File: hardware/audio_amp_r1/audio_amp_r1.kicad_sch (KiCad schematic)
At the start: 24 parts, among them J1 PJ-320D, J2 PJ-320D, J3 JST_PH_1x02, J4 Conn_01x04_Pin, J5 Conn_01x04_Pin, J6 KH-BNC50-3511, J7 KH-BNC50-3511, U1 AD8397

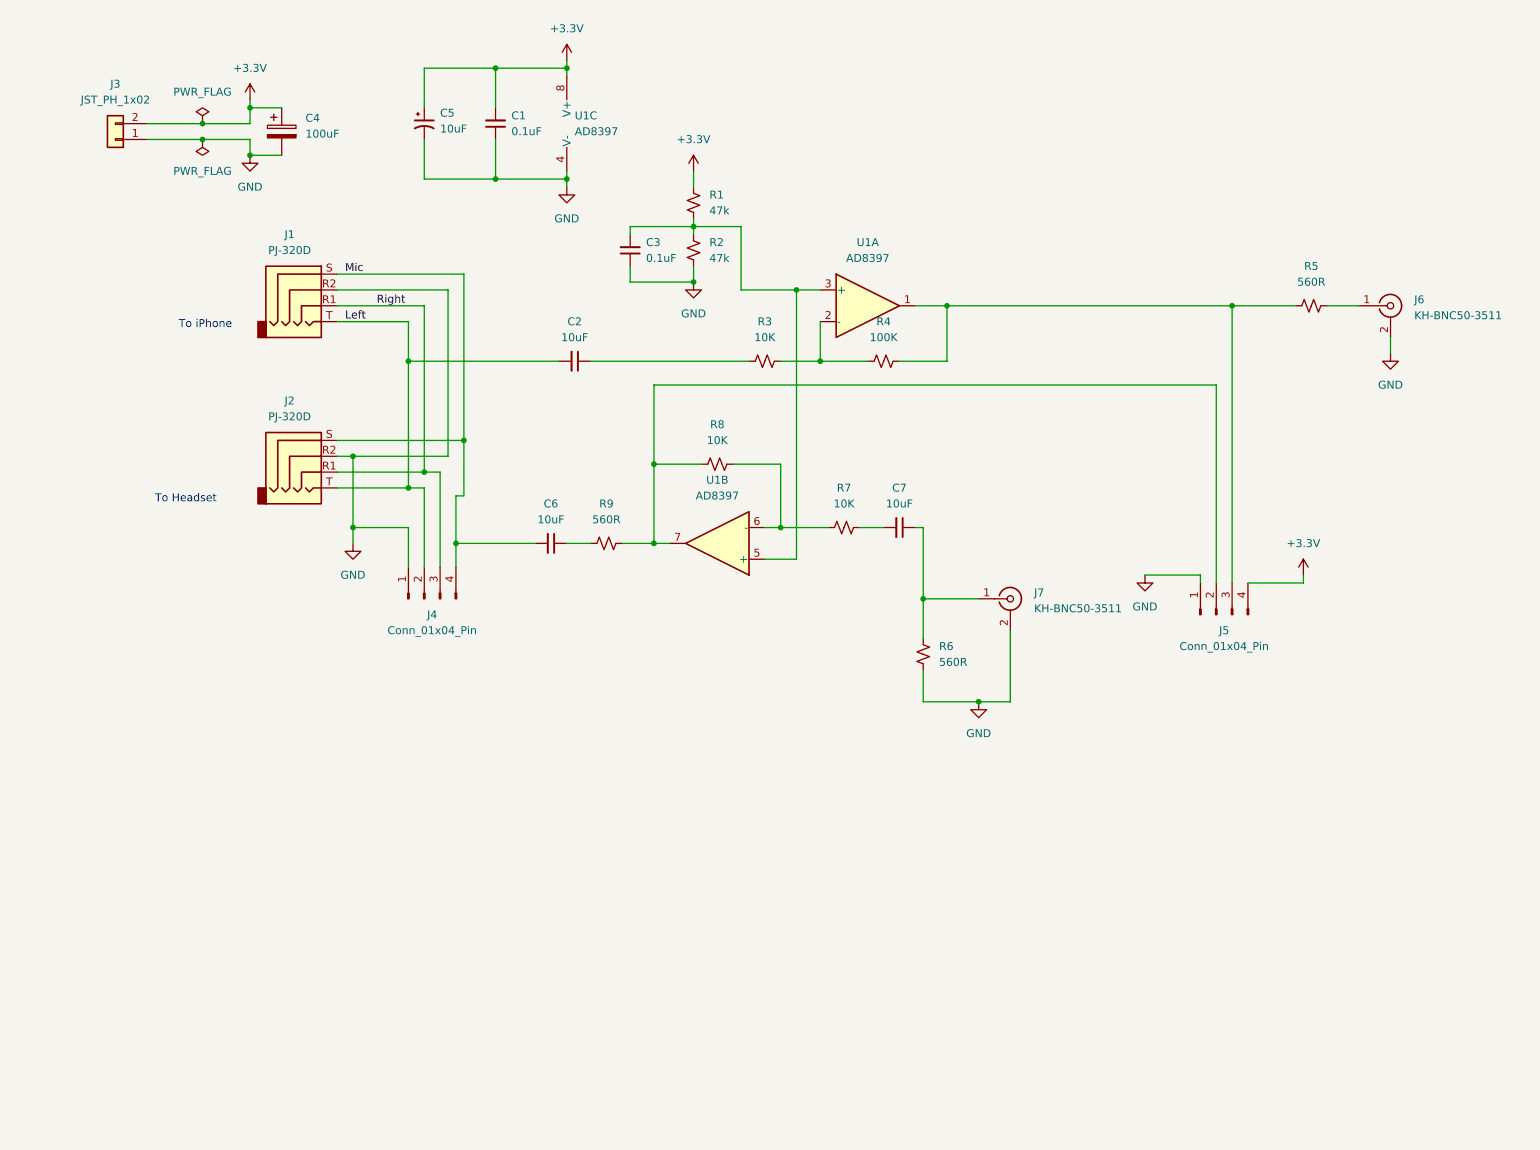
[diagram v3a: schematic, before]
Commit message: update circuit to drive mic
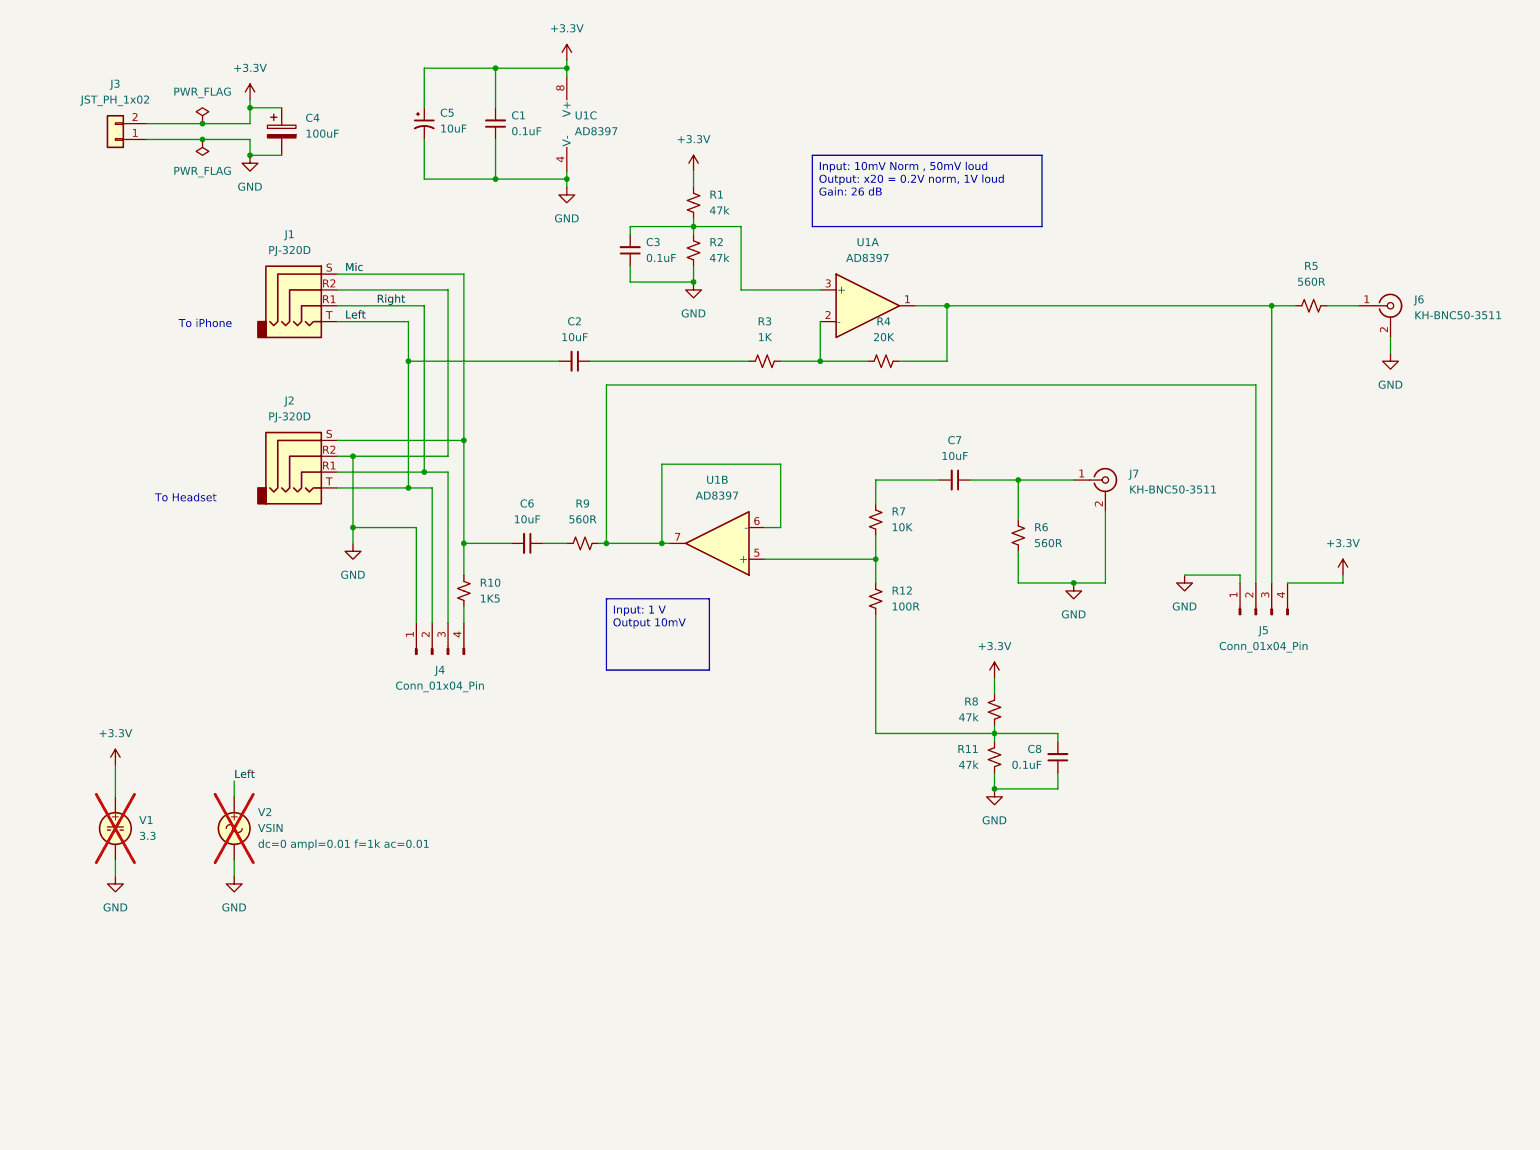
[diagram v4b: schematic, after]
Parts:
- added C8: 0.1uF, Capacitor_SMD:C_0805_2012Metric, symbol Device:C_Small
- added R10: 1K5, Resistor_SMD:R_0805_2012Metric, symbol Device:R_Small_US
- added R11: 47k, Resistor_SMD:R_0805_2012Metric, symbol Device:R_Small_US
- added R12: 100R, Resistor_SMD:R_0805_2012Metric, symbol Device:R_Small_US
- added V1: 3.3, symbol Simulation_SPICE:VDC
- added V2: VSIN, symbol Simulation_SPICE:VSIN
- R3: value 10K -> 1K; JLCPCB Part # C17414 -> (none)
- R4: value 100K -> 20K; JLCPCB Part # C149504 -> (none)
- R8: value 10K -> 47k; JLCPCB Part # C17414 -> C17713
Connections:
- net +3.3V: now also R8.2, V1.1
- net GND: now also C8.1, R11.1, V1.2, V2.2
- net Left: now also V2.1
- net Mic: now also R10.2; no longer J4.4 (Pin_4)
- net at J5.2 (Pin_2), R9.2, U1.7: now also U1.6 (-); no longer R8.2
- net at C3.2, R1.1, R2.2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: no longer U1.5 (+)
- new net: C8.2, R11.2, R12.2, R8.1
- new net: R12.1, R7.2, U1.5 (+)
- new net: J4.4 (Pin_4), R10.1
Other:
- moved on the sheet: C6, C7, J4, J5, J7, R6, R7, R9

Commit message: update prod files
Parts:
- added J8: Conn_01x04_Pin, Connector_PinHeader_2.54mm:PinHeader_1x04_P2.54mm_Vertical_SMD_Pin1Left, symbol Connector:Conn_01x04_Pin
- J4, J5: JLCPCB Part # C2881610 -> C5160787
- R10: JLCPCB Part # (none) -> C4310
- R12: JLCPCB Part # (none) -> C17408
- R3: JLCPCB Part # (none) -> C17513
- R4: value 20K -> 22K; JLCPCB Part # (none) -> C17560
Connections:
- net at C8.2, R11.2, R12.2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: now also J8.4 (Pin_4)
- net at J5.3 (Pin_3), R4.1, R5.2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: now also J8.2 (Pin_2)
- net at R3.1, R4.2, U1.2 (-): now also J8.1 (Pin_1)
- net at R12.1, R7.2, U1.5 (+): now also J8.3 (Pin_3)
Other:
- moved on the sheet: R12, U1B

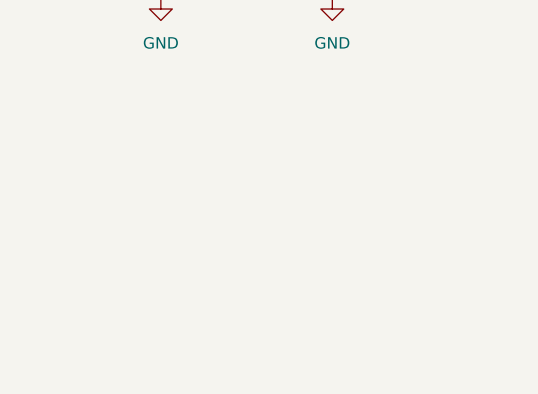
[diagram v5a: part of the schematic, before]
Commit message: update with tool holes and labels
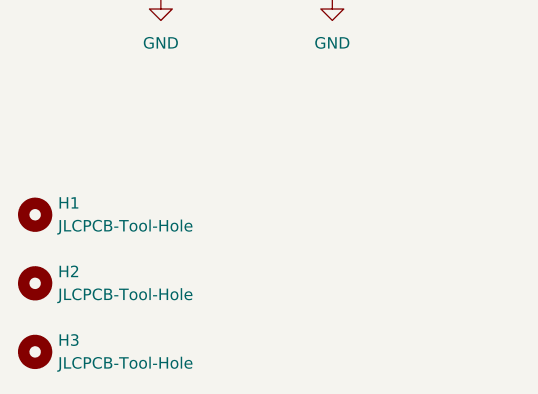
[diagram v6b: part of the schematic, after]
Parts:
- added H1, H2, H3: JLCPCB-Tool-Hole, FootprintLib:MountingHole_JLCPCB_Tool, symbol Mechanical:MountingHole
- J4, J5, J8: JLCPCB Part # C5160787 -> C2883761
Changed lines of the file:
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@@
+    )
+  )
+  (symbol (lib_id "Mechanical:MountingHole") (at 29.21 191.77 0) (unit 1)
+    (in_bom yes) (on_board yes) (dnp no) (fields_autoplaced)
+    (property "Reference" "H3" (at 31.75 190.5 0)
+      (effects (font (size 1.27 1.27)) (justify left))
+    )
+    (property "Value" "JLCPCB-Tool-Hole" (at 31.75 193.04 0)
+      (effects (font (size 1.27 1.27)) (justify left))
+    )
+    (property "Footprint" "FootprintLib:MountingHole_JLCPCB_Tool" (at 29.21 191.77 0)
+      (effects (font (size 1.27 1.27)) hide)
+    )
+    (property "Datasheet" "~" (at 29.21 191.77 0)
+      (effects (font (size 1.27 1.27)) hide)
+    )
+    (instances
+      (project "audio_amp_r1"
+        (path "/65a2a7ad-257a-48a0-a706-3da4b4be7c88"
+          (reference "H3") (unit 1)
+        )
+      )
     )
   )
@@
       (effects (font (size 1.27 1.27)) hide)
     )
-    (property "JLCPCB Part #" "C5160787" (at 149.86 82.55 0)
+    (property "JLCPCB Part #" "C2883761" (at 149.86 82.55 0)
       (effects (font (size 1.27 1.27)) hide)
     )
@@
     )
   )
+  (symbol (lib_id "Mechanical:MountingHole") (at 29.21 176.53 0) (unit 1)
+    (in_bom yes) (on_board yes) (dnp no) (fields_autoplaced)
+    (property "Reference" "H1" (at 31.75 175.26 0)
+      (effects (font (size 1.27 1.27)) (justify left))
+    )
+    (property "Value" "JLCPCB-Tool-Hole" (at 31.75 177.8 0)
+      (effects (font (size 1.27 1.27)) (justify left))
+    )
+    (property "Footprint" "FootprintLib:MountingHole_JLCPCB_Tool" (at 29.21 176.53 0)
+      (effects (font (size 1.27 1.27)) hide)
+    )
+    (property "Datasheet" "~" (at 29.21 176.53 0)
+      (effects (font (size 1.27 1.27)) hide)
+    )
+    (instances
+      (project "audio_amp_r1"
+        (path "/65a2a7ad-257a-48a0-a706-3da4b4be7c88"
+          (reference "H1") (unit 1)
+        )
+      )
+    )
+  )
   (symbol (lib_id "Connector:Conn_01x04_Pin") (at 226.06 110.49 90) (unit 1)
     (in_bom yes) (on_board yes) (dnp no) (fields_autoplaced)
@@
       (effects (font (size 1.27 1.27)) hide)
     )
-    (property "JLCPCB Part #" "C5160787" (at 226.06 110.49 0)
+    (property "JLCPCB Part #" "C2883761" (at 226.06 110.49 0)
       (effects (font (size 1.27 1.27)) hide)
     )
@@
     )
   )
+  (symbol (lib_id "Mechanical:MountingHole") (at 29.21 184.15 0) (unit 1)
+    (in_bom yes) (on_board yes) (dnp no) (fields_autoplaced)
+    (property "Reference" "H2" (at 31.75 182.88 0)
+      (effects (font (size 1.27 1.27)) (justify left))
+    )
+    (property "Value" "JLCPCB-Tool-Hole" (at 31.75 185.42 0)
+      (effects (font (size 1.27 1.27)) (justify left))
+    )
+    (property "Footprint" "FootprintLib:MountingHole_JLCPCB_Tool" (at 29.21 184.15 0)
+      (effects (font (size 1.27 1.27)) hide)
+    )
+    (property "Datasheet" "~" (at 29.21 184.15 0)
+      (effects (font (size 1.27 1.27)) hide)
+    )
+    (instances
+      (project "audio_amp_r1"
+        (path "/65a2a7ad-257a-48a0-a706-3da4b4be7c88"
+          (reference "H2") (unit 1)
+        )
+      )
+    )
+  )
   (symbol (lib_id "Device:R_Small_US") (at 135.89 44.45 180) (unit 1)
     (in_bom yes) (on_board yes) (dnp no) (fields_autoplaced)
@@
       (effects (font (size 1.27 1.27)) hide)
     )
-    (property "JLCPCB Part #" "C5160787" (at 93.98 116.84 0)
-      (effects (font (size 1.27 1.27)) hide)
-    )
+    (property "JLCPCB Part #" "C2883761" (at 93.98 116.84 0)
+      (effects (font (size 1.27 1.27)) hide)
+    )

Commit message: update prod
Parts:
- H1, H2, H3: now not fitted; now left out of the parts list
- J1, J2: footprint Connector_Audio:Jack_3.5mm_PJ320D_Horizontal -> FootprintLib:Jack_3.5mm_PJ320D_Horizontal-CJ
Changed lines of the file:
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@@
   )
   (symbol (lib_id "Mechanical:MountingHole") (at 29.21 191.77 0) (unit 1)
-    (in_bom yes) (on_board yes) (dnp no) (fields_autoplaced)
+    (in_bom no) (on_board yes) (dnp yes) (fields_autoplaced)
     (property "Reference" "H3" (at 31.75 190.5 0)
       (effects (font (size 1.27 1.27)) (justify left))
@@
     )
     (property "Datasheet" "~" (at 29.21 191.77 0)
+      (effects (font (size 1.27 1.27)) hide)
+    )
+    (property "Sim.Enable" "0" (at 29.21 191.77 0)
       (effects (font (size 1.27 1.27)) hide)
     )
@@
   )
   (symbol (lib_id "Mechanical:MountingHole") (at 29.21 176.53 0) (unit 1)
-    (in_bom yes) (on_board yes) (dnp no) (fields_autoplaced)
+    (in_bom no) (on_board yes) (dnp yes) (fields_autoplaced)
     (property "Reference" "H1" (at 31.75 175.26 0)
       (effects (font (size 1.27 1.27)) (justify left))
@@
     )
     (property "Datasheet" "~" (at 29.21 176.53 0)
+      (effects (font (size 1.27 1.27)) hide)
+    )
+    (property "Sim.Enable" "0" (at 29.21 176.53 0)
       (effects (font (size 1.27 1.27)) hide)
     )
@@
   )
   (symbol (lib_id "Mechanical:MountingHole") (at 29.21 184.15 0) (unit 1)
-    (in_bom yes) (on_board yes) (dnp no) (fields_autoplaced)
+    (in_bom no) (on_board yes) (dnp yes) (fields_autoplaced)
     (property "Reference" "H2" (at 31.75 182.88 0)
       (effects (font (size 1.27 1.27)) (justify left))
@@
     )
     (property "Datasheet" "~" (at 29.21 184.15 0)
+      (effects (font (size 1.27 1.27)) hide)
+    )
+    (property "Sim.Enable" "0" (at 29.21 184.15 0)
       (effects (font (size 1.27 1.27)) hide)
     )
@@
       (effects (font (size 1.27 1.27)))
     )
-    (property "Footprint" "Connector_Audio:Jack_3.5mm_PJ320D_Horizontal" (at 73.66 58.42 0)
+    (property "Footprint" "FootprintLib:Jack_3.5mm_PJ320D_Horizontal-CJ" (at 73.66 58.42 0)
       (effects (font (size 1.27 1.27)) hide)
     )
@@
       (effects (font (size 1.27 1.27)))
     )
-    (property "Footprint" "Connector_Audio:Jack_3.5mm_PJ320D_Horizontal" (at 73.66 85.09 0)
-      (effects (font (size 1.27 1.27)) hide)
-    )
+    (property "Footprint" "FootprintLib:Jack_3.5mm_PJ320D_Horizontal-CJ" (at 73.66 85.09 0)
+      (effects (font (size 1.27 1.27)) hide)
+    )

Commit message: sent to prod
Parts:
- J6, J7: footprint Connector_Coaxial:BNC_Amphenol_B6252HB-NPP3G-50_Horizontal -> FootprintLib:BNC_Amphenol_B6252HB-NPP3G-50_Horizontal-CJ
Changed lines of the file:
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@@
       (effects (font (size 1.27 1.27)) (justify left))
     )
-    (property "Footprint" "Connector_Coaxial:BNC_Amphenol_B6252HB-NPP3G-50_Horizontal" (at 201.93 88.9 0)
+    (property "Footprint" "FootprintLib:BNC_Amphenol_B6252HB-NPP3G-50_Horizontal-CJ" (at 201.93 88.9 0)
       (effects (font (size 1.27 1.27)) hide)
     )
@@
       (effects (font (size 1.27 1.27)) (justify left))
     )
-    (property "Footprint" "Connector_Coaxial:BNC_Amphenol_B6252HB-NPP3G-50_Horizontal" (at 247.65 60.96 0)
+    (property "Footprint" "FootprintLib:BNC_Amphenol_B6252HB-NPP3G-50_Horizontal-CJ" (at 247.65 60.96 0)
       (effects (font (size 1.27 1.27)) hide)
     )
